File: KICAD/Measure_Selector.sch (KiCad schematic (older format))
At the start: 2 parts, among them U3 CD4053BM96

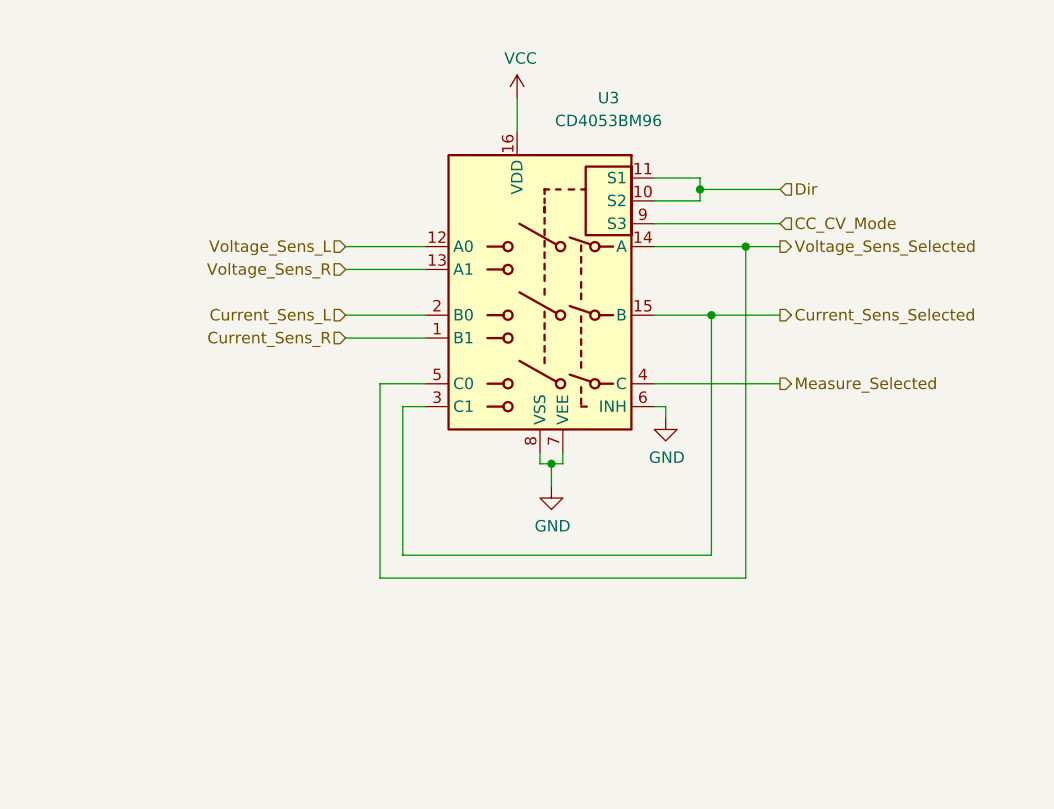
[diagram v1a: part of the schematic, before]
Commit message: drivers draft + clean and minors changes
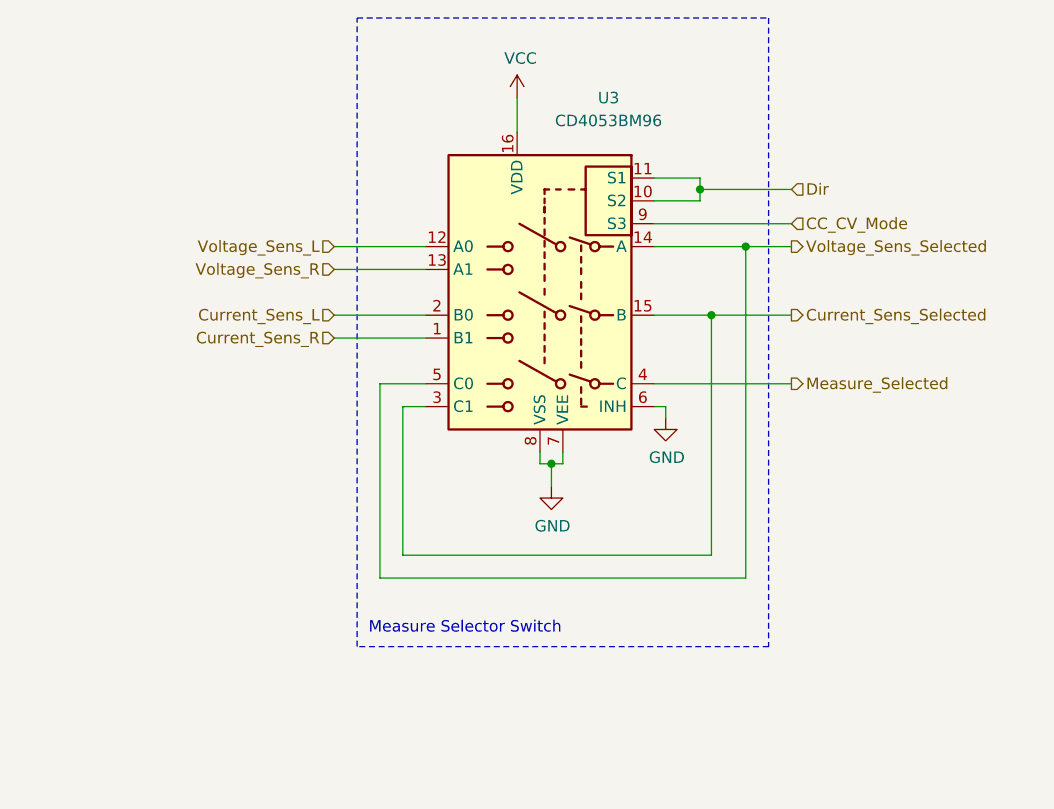
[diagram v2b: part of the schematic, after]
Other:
- note added: "Measure Selector Switch"
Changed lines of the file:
@@
 Comment4 ""
 $EndDescr
-Text HLabel 5250 3450 0    50   Input ~ 0
+Text HLabel 5200 3450 0    50   Input ~ 0
 Voltage_Sens_R
-Text HLabel 5250 3750 0    50   Input ~ 0
+Text HLabel 5200 3750 0    50   Input ~ 0
 Current_Sens_R
-Text HLabel 5250 3350 0    50   Input ~ 0
+Text HLabel 5200 3350 0    50   Input ~ 0
 Voltage_Sens_L
-Text HLabel 5250 3650 0    50   Input ~ 0
+Text HLabel 5200 3650 0    50   Input ~ 0
 Current_Sens_L
-Text HLabel 7150 3350 2    50   Output ~ 0
+Text HLabel 7200 3350 2    50   Output ~ 0
 Voltage_Sens_Selected
-Text HLabel 7150 3650 2    50   Output ~ 0
+Text HLabel 7200 3650 2    50   Output ~ 0
 Current_Sens_Selected
-Text HLabel 7150 3250 2    50   Input ~ 0
+Text HLabel 7200 3250 2    50   Input ~ 0
 CC_CV_Mode
-Text HLabel 7150 3100 2    50   Input ~ 0
+Text HLabel 7200 3100 2    50   Input ~ 0
 Dir
-Text HLabel 7150 3950 2    50   Output ~ 0
+Text HLabel 7200 3950 2    50   Output ~ 0
 Measure_Selected
 $Comp
@@
 	6150 4300 6100 4300
 Wire Wire Line
-	6600 3950 7150 3950
+	6600 3950 7200 3950
 Wire Wire Line
 	6600 3650 6850 3650
@@
 	6600 3350 7000 3350
 Wire Wire Line
-	6600 3250 7150 3250
+	6600 3250 7200 3250
 Wire Wire Line
-	6800 3100 7150 3100
+	6800 3100 7200 3100
 Wire Wire Line
 	6000 2700 6000 2850
@@
 	5600 4050 5500 4050
 Wire Wire Line
-	5600 3350 5250 3350
+	5600 3350 5200 3350
 Wire Wire Line
-	5250 3450 5600 3450
+	5200 3450 5600 3450
 Wire Wire Line
-	5600 3650 5250 3650
+	5600 3650 5200 3650
 Wire Wire Line
-	5250 3750 5600 3750
+	5200 3750 5600 3750
 $Comp
 L power:GND #PWR0162
@@
 Connection ~ 6850 3650
 Wire Wire Line
-	6850 3650 7150 3650
+	6850 3650 7200 3650
 Wire Wire Line
 	5400 3950 5400 4800
@@
 Connection ~ 7000 3350
 Wire Wire Line
-	7000 3350 7150 3350
+	7000 3350 7200 3350
+Wire Notes Line
+	7100 5100 5300 5100
+Wire Notes Line
+	5300 5100 5300 2350
+Wire Notes Line
+	5300 2350 7100 2350
+Wire Notes Line
+	7100 2350 7100 5100
+Text Notes 5350 5050 0    50   ~ 0
+Measure Selector Switch
 $EndSCHEMATC

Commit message: review w/ jmt
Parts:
- U3: footprint Package_SO:SO-16_3.9x9.9mm_P1.27mm -> (none)
- gave numbers to parts that had none: 1
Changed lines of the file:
@@
 F 0 "U3" H 5800 4400 50  0000 C CNN
 F 1 "CD4053BM96" H 5800 4300 50  0000 C CNN
-F 2 "Package_SO:SO-16_3.9x9.9mm_P1.27mm" H 6250 2800 50  0001 L CNN
+F 2 "" H 6250 2800 50  0001 L CNN
 F 3 "http://www.ti.com/lit/ds/symlink/cd4052b.pdf" H 6080 3750 50  0001 C CNN
 	1    6100 3550
@@
 	6800 3100 6800 3150
 $Comp
-L power:GND #PWR0161
+L power:GND #PWR036
 U 1 1 610E2D38
 P 6650 4100
-F 0 "#PWR0161" H 6650 3850 50  0001 C CNN
+F 0 "#PWR036" H 6650 3850 50  0001 C CNN
 F 1 "GND" H 6655 3927 50  0000 C CNN
 F 2 "" H 6650 4100 50  0001 C CNN
@@
 	5200 3750 5600 3750
 $Comp
-L power:GND #PWR0162
+L power:GND #PWR035
 U 1 1 610C24DF
 P 6150 4400
-F 0 "#PWR0162" H 6150 4150 50  0001 C CNN
+F 0 "#PWR035" H 6150 4150 50  0001 C CNN
 F 1 "GND" H 6155 4227 50  0000 C CNN
 F 2 "" H 6150 4400 50  0001 C CNN
@@
 $EndComp
 $Comp
-L power:GND #PWR0163
+L power:GND #PWR033
 U 1 1 61122566
 P 750 7450
-F 0 "#PWR0163" H 750 7200 50  0001 C CNN
+F 0 "#PWR033" H 750 7200 50  0001 C CNN
 F 1 "GND" H 755 7277 50  0000 C CNN
 F 2 "" H 750 7450 50  0001 C CNN
@@
 $EndComp
 $Comp
-L Device:C C?
+L Device:C C12
 U 1 1 6112299E
 P 750 7300
-F 0 "C?" H 865 7346 50  0000 L CNN
+F 0 "C12" H 865 7346 50  0000 L CNN
 F 1 "100n" H 865 7255 50  0000 L CNN
 F 2 "" H 788 7150 50  0001 C CNN
@@
 $EndComp
 $Comp
-L power:VCC #PWR0164
+L power:VCC #PWR032
 U 1 1 61547D97
 P 750 7150
-F 0 "#PWR0164" H 750 7000 50  0001 C CNN
+F 0 "#PWR032" H 750 7000 50  0001 C CNN
 F 1 "VCC" H 765 7323 50  0000 C CNN
 F 2 "" H 750 7150 50  0001 C CNN
@@
 $EndComp
 $Comp
-L power:VCC #PWR0165
+L power:VCC #PWR034
 U 1 1 61549B3F
 P 6000 2700
-F 0 "#PWR0165" H 6000 2550 50  0001 C CNN
+F 0 "#PWR034" H 6000 2550 50  0001 C CNN
 F 1 "VCC" H 6015 2873 50  0000 C CNN
 F 2 "" H 6000 2700 50  0001 C CNN

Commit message: edit footprints by jmt
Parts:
- C12: footprint (none) -> Capacitor_SMD:C_0805_2012Metric_Pad1.15x1.40mm_HandSolder
- U3: footprint (none) -> Package_SO:SOIC-16_4.55x10.3mm_P1.27mm
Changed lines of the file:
@@
 F 0 "U3" H 5800 4400 50  0000 C CNN
 F 1 "CD4053BM96" H 5800 4300 50  0000 C CNN
-F 2 "" H 6250 2800 50  0001 L CNN
+F 2 "Package_SO:SOIC-16_4.55x10.3mm_P1.27mm" H 6250 2800 50  0001 L CNN
 F 3 "http://www.ti.com/lit/ds/symlink/cd4052b.pdf" H 6080 3750 50  0001 C CNN
 	1    6100 3550
@@
 F 0 "C12" H 865 7346 50  0000 L CNN
 F 1 "100n" H 865 7255 50  0000 L CNN
-F 2 "" H 788 7150 50  0001 C CNN
+F 2 "Capacitor_SMD:C_0805_2012Metric_Pad1.15x1.40mm_HandSolder" H 788 7150 50  0001 C CNN
 F 3 "~" H 750 7300 50  0001 C CNN
 	1    750  7300

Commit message: added footprint for sepic coil + no more errors in netlist
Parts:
- C12: footprint Capacitor_SMD:C_0805_2012Metric_Pad1.15x1.40mm_HandSolder -> Sesame_footprint:C_0805_2012Metric_Pad1.18x1.45mm_HandSolder
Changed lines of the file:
@@
 F 0 "C12" H 865 7346 50  0000 L CNN
 F 1 "100n" H 865 7255 50  0000 L CNN
-F 2 "Capacitor_SMD:C_0805_2012Metric_Pad1.15x1.40mm_HandSolder" H 788 7150 50  0001 C CNN
+F 2 "Sesame_footprint:C_0805_2012Metric_Pad1.18x1.45mm_HandSolder" H 788 7150 50  0001 C CNN
 F 3 "~" H 750 7300 50  0001 C CNN
 	1    750  7300

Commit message: 200 conn. remaining
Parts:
- U3: footprint Package_SO:SOIC-16_4.55x10.3mm_P1.27mm -> Package_SO:SOIC-16_3.9x9.9mm_P1.27mm
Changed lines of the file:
@@
 F 0 "U3" H 5800 4400 50  0000 C CNN
 F 1 "CD4053BM96" H 5800 4300 50  0000 C CNN
-F 2 "Package_SO:SOIC-16_4.55x10.3mm_P1.27mm" H 6250 2800 50  0001 L CNN
+F 2 "Package_SO:SOIC-16_3.9x9.9mm_P1.27mm" H 6250 2800 50  0001 L CNN
 F 3 "http://www.ti.com/lit/ds/symlink/cd4052b.pdf" H 6080 3750 50  0001 C CNN
 	1    6100 3550

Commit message: lil cleanup on the main schematic sheet
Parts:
- C12: symbol Device:C -> sesame-fonctionnel-rescue:C-Device
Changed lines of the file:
@@
 	6800 3100 6800 3150
 $Comp
-L power:GND #PWR036
+L sesame-fonctionnel-rescue:GND-power #PWR036
 U 1 1 610E2D38
 P 6650 4100
@@
 	5200 3750 5600 3750
 $Comp
-L power:GND #PWR035
+L sesame-fonctionnel-rescue:GND-power #PWR035
 U 1 1 610C24DF
 P 6150 4400
@@
 $EndComp
 $Comp
-L power:GND #PWR033
+L sesame-fonctionnel-rescue:GND-power #PWR033
 U 1 1 61122566
 P 750 7450
@@
 $EndComp
 $Comp
-L Device:C C12
+L sesame-fonctionnel-rescue:C-Device C12
 U 1 1 6112299E
 P 750 7300
@@
 $EndComp
 $Comp
-L power:VCC #PWR032
+L sesame-fonctionnel-rescue:VCC-power #PWR032
 U 1 1 61547D97
 P 750 7150
@@
 $EndComp
 $Comp
-L power:VCC #PWR034
+L sesame-fonctionnel-rescue:VCC-power #PWR034
 U 1 1 61549B3F
 P 6000 2700
